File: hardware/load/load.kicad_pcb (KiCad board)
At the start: 2 copper layers, 25 x 30 mm, 25 parts, among them J1 PH2-12-UA, J2 B3B-XH-A, J3 Conn_01x07, J4 Conn_01x07, J5 B2B-XH-A, J6 B2B-XH-A, Q1 DMG2301L, Q2 MMBT3904, Q3 DMG2301L, Q4 MMBT3904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

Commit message: Finishing touches for v2
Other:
- board text added: "github.com/j9brown/minuet Brown Studios Minuet Lighting and Load Accessory 2025/2, v2.0"
- board text removed: "github.com/j9brown/minuet Brown Studios Minuet Lighting and Load Accessory 2024/2, v2.0"

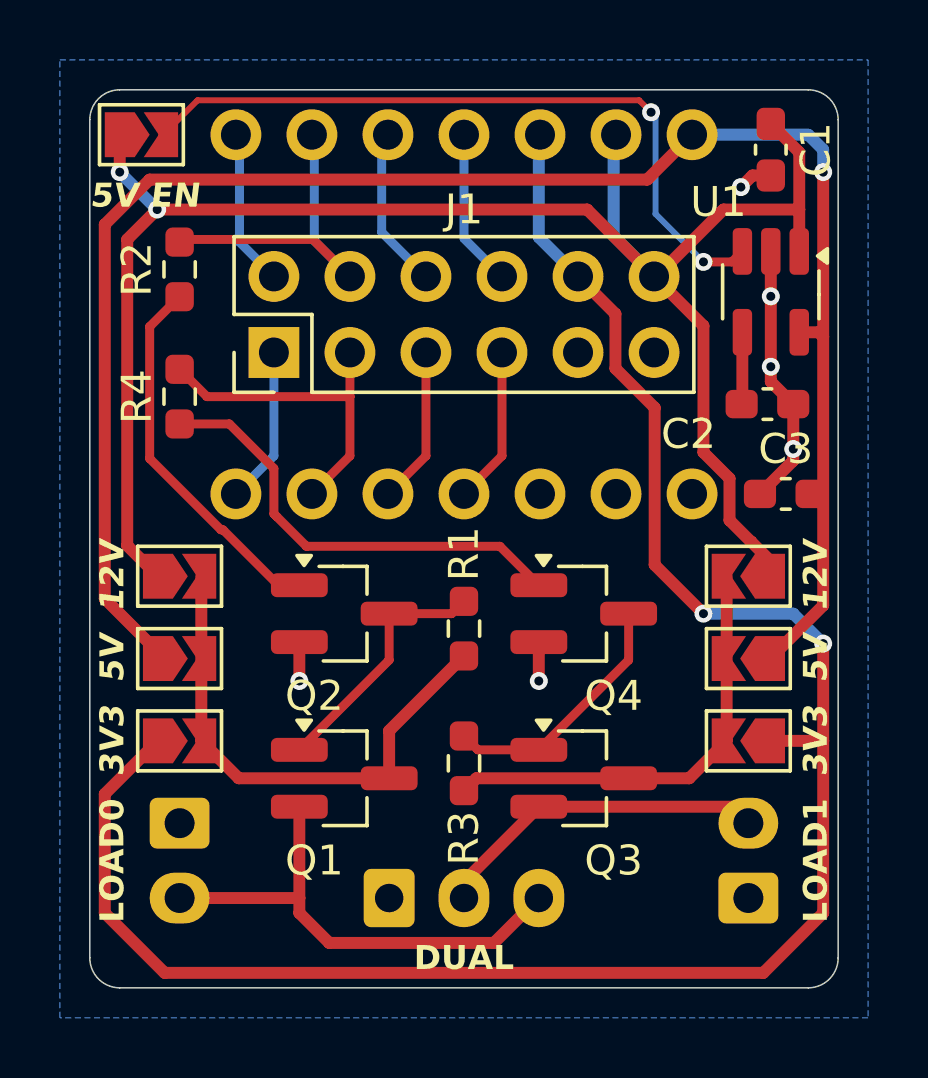
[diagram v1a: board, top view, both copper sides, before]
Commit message: Abandon load accessory design, update errata.
Decided to abandon this design because it is overly complex and
doesn't work with addressable LEDs as intended.  It would be better
to design simpler boards for each use-case instead of having lots
of jumpers.
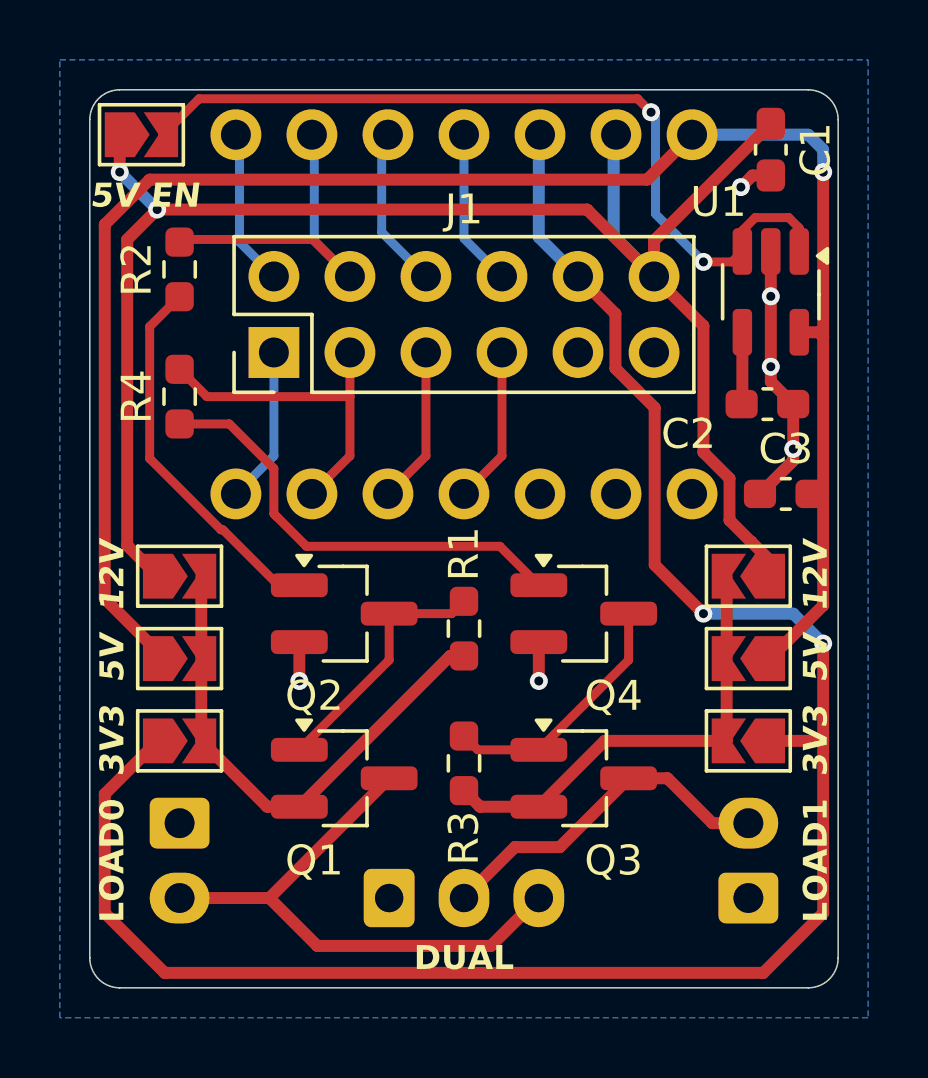
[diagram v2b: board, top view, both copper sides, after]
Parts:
- R1, R3: value 100K -> 10K
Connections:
- Q1 pad 2: /LOAD0 -> Net-(JP2-B)
- Q1 pad 3: Net-(JP2-B) -> /LOAD0
- Q3 pad 2: /LOAD1 -> Net-(JP5-B)
- Q3 pad 3: Net-(JP5-B) -> /LOAD1
- U1 pad 1: +12V -> Net-(JP1-B)
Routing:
- net Net-(JP1-B): track 24.1 -> 27.9 mm
- net +12V: track 60.3 -> 56.7 mm
- net /LOAD0: track 16.6 -> 19.0 mm
- net /LOAD1: track 10.8 -> 11.8 mm
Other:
- board text added: "github.com/j9brown/minuet Brown Studios Minuet Lighting and Load Accessory 2025/2, v2.1"
- board text removed: "github.com/j9brown/minuet Brown Studios Minuet Lighting and Load Accessory 2025/2, v2.0"
